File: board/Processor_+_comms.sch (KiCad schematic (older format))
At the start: 43 parts, among them J1 53261-0471, U11 ATXMEGA256A3U-MH, U12 NTS0104, U14 TC1015-3.3VCT713

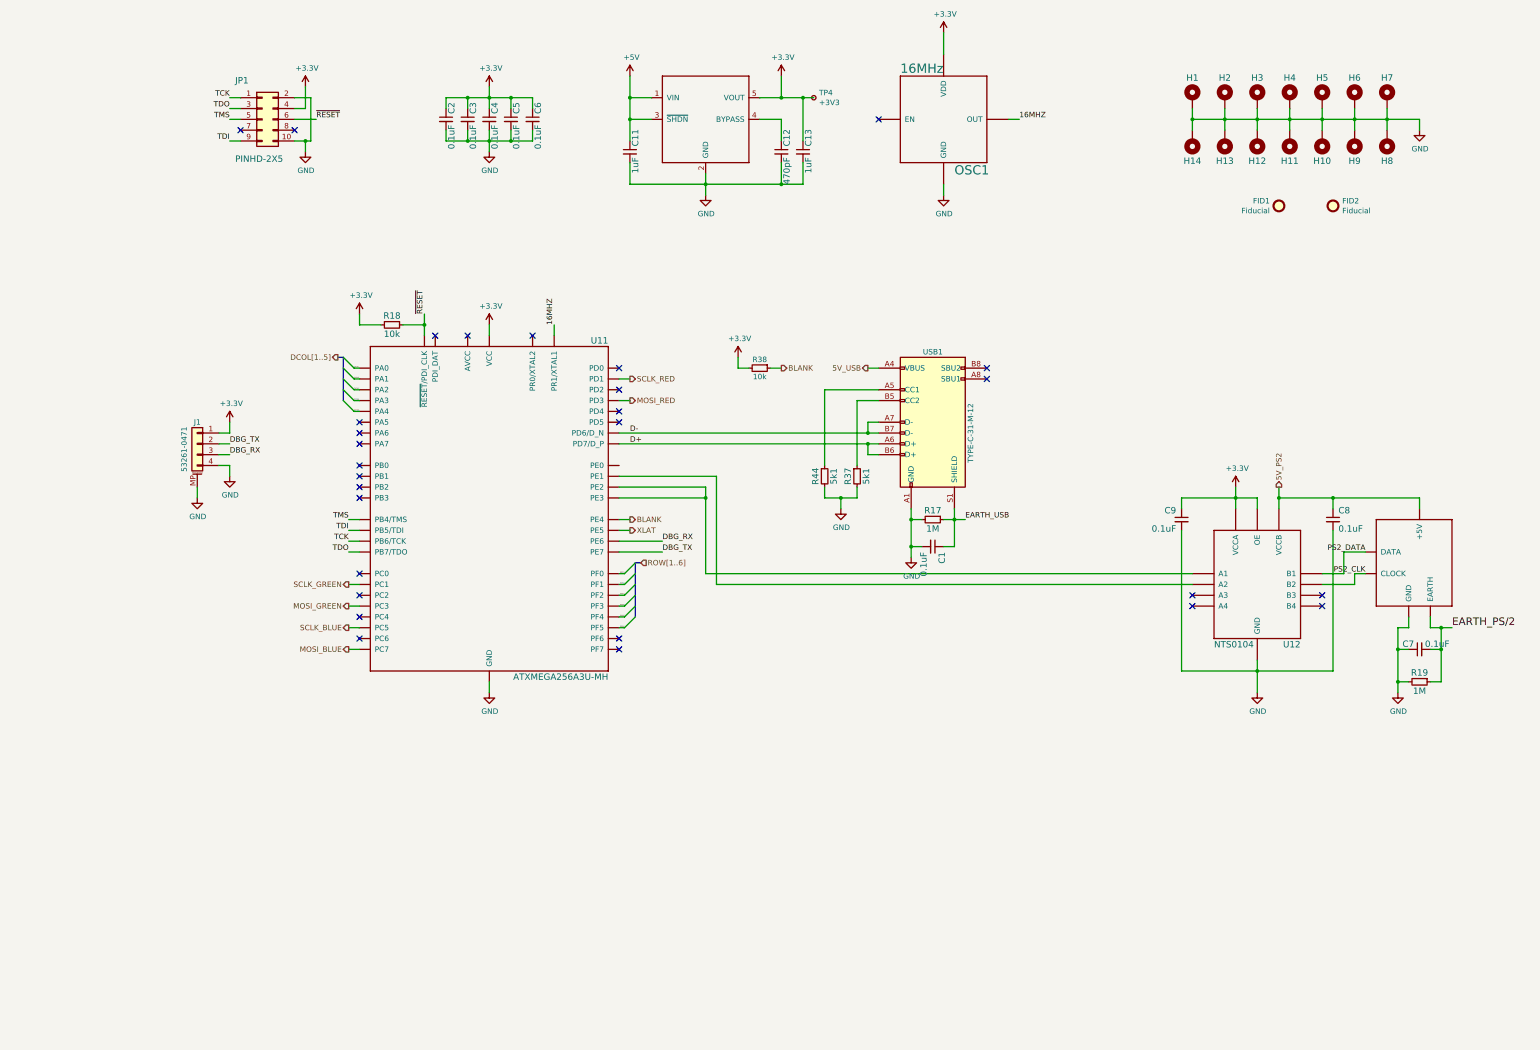
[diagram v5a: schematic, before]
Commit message: Added handling to the board for USB-PD and USB BC v1.2 so we can legally use all 1A we can potentially draw
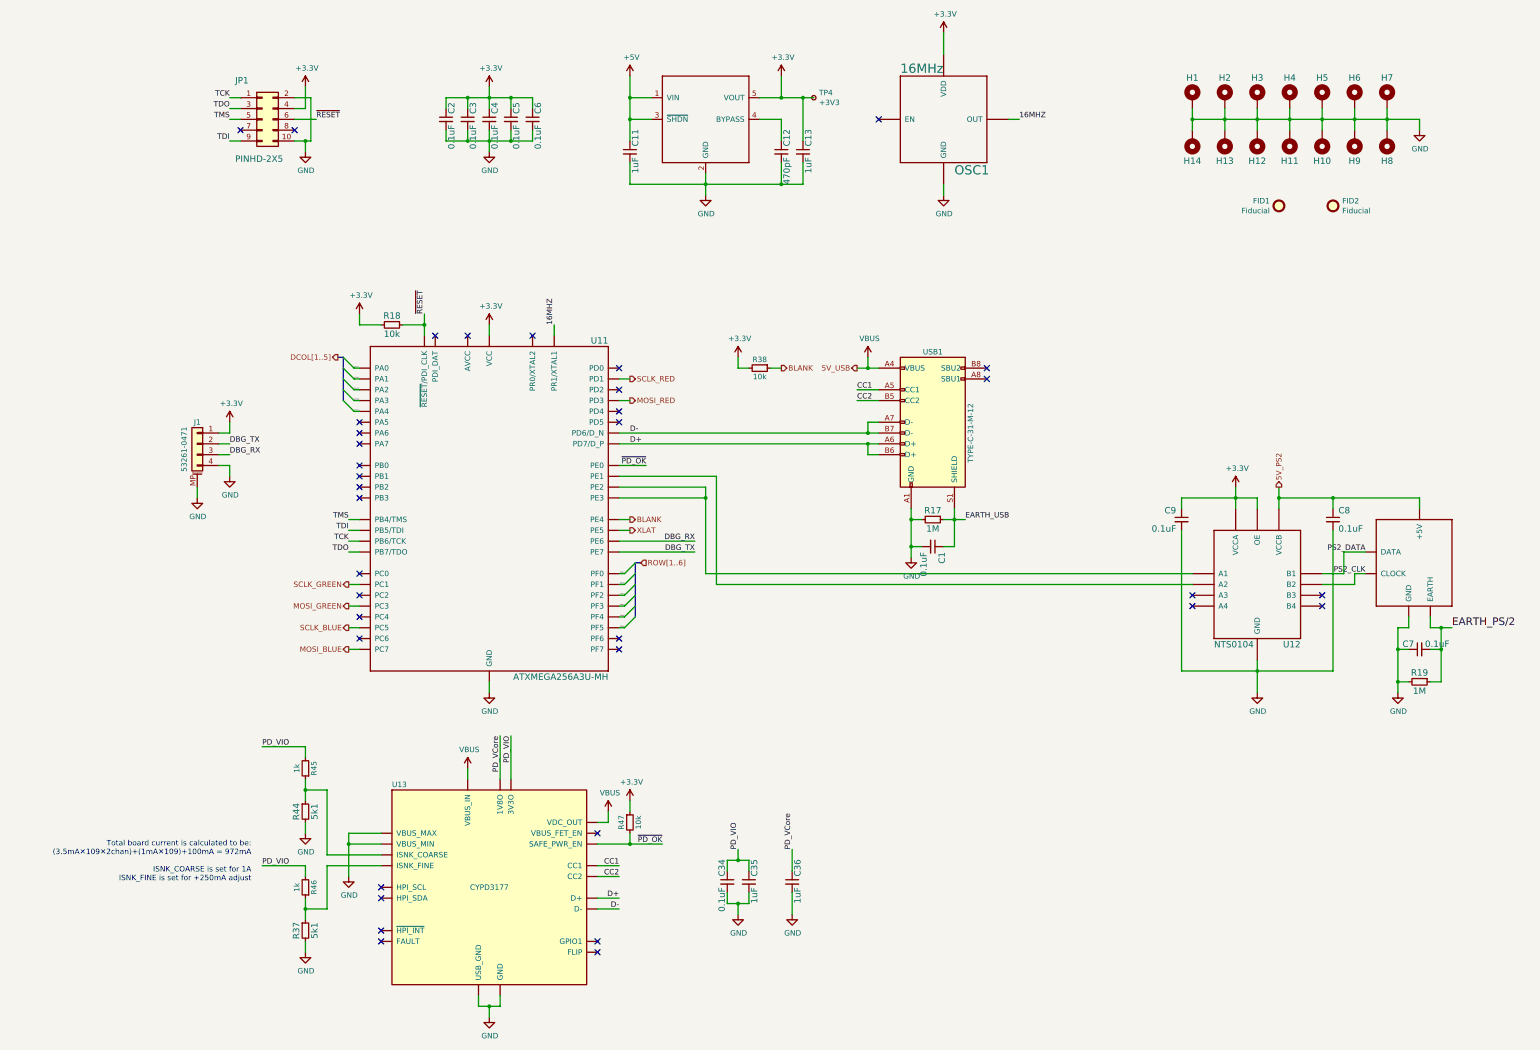
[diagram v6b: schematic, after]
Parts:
- added C34: 0.1uF, rhais_rcl:C0603, symbol Device:C_Small
- added C35, C36: 1uF, rhais_rcl:C0603, symbol Device:C_Small
- added R45, R46: 1k, rhais_rcl:R0603, symbol Device:R_Small
- added R47: 10k, rhais_rcl:R0603, symbol Device:R_Small
- added U13: CYPD3177, rhais_package-qfn:QFN-24-1EP_4x4mm_P0.5mm_EP2.6x2.6mm, symbol DX_MON:CYPD3177
- R37, R44: MPN MCWR06X1003FTL -> MCWR06X5101FTL; OC_FARNELL 2447226 -> 2447404; URL_FARNELL https://uk.farnell.com/multicomp/mcwr06x1003ftl/res-100k-1-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 -> https://uk.farnell.com/multicomp/mcwr06x5101ftl/res-5k1-1-0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
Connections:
- net +3V3: now also R47.1
- net D+: now also U13.17 (D+)
- net D-: now also U13.16 (D-)
- net GND: now also C34.2, C35.2, C36.2, U13.1 (VBUS_MIN), U13.19 (GND), U13.2 (VBUS_MAX), U13.22 (USB_GND), U13.25 (EPAD)
- net ~PD_OK: now reaches U11.36 (PE0)
- net ~PD_OK: now also R47.2, U13.4 (SAFE_PWR_EN)
- net at R44.1: now also R45.1, U13.5 (ISNK_COARSE); no longer USB1.A5 (CC1)
- net at R37.1: now also R46.1, U13.6 (ISNK_FINE); no longer USB1.B5 (CC2)
- net 5V_USB renamed VBUS
- net VBUS: now also U13.11 (VDC_OUT), U13.18 (VBUS_IN)
- new net CC1: U13.15 (CC1), USB1.A5 (CC1)
- new net CC2: U13.14 (CC2), USB1.B5 (CC2)
- new net PD_VCore: C36.1, U13.24 (1V8O)
- new net PD_VIO: C34.1, C35.1, R45.2, R46.2, U13.23 (3V3O)
- no-connect marks 29 -> 36
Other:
- note added: "Total board current is calculated to be:\n(3.5mA✕109✕2chan)+(1mA✕109)+100mA = 972mA\n\nISNK_COARSE is set for 1A\nISNK_FINE is set for +250mA adjust"
- moved on the sheet: R37, R44

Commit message: Fixed some ERC issues
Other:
- moved on the sheet: R38
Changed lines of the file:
@@
 	1    0    0    -1
 $EndComp
-Text HLabel 8400 4500 2    50   Output ~ 0
+Text HLabel 8200 4500 2    50   Output ~ 0
 BLANK
 $Comp
 L Device:R_Small R38
 U 1 1 6F58D17A
-P 8200 4500
-F 0 "R38" V 8150 4500 50  0000 C BNN
-F 1 "10k" V 8250 4500 50  0000 C TNN
-F 2 "rhais_rcl:R0603" H 8200 4500 50  0001 C CNN
-F 3 "http://www.farnell.com/datasheets/2860681.pdf" H 8200 4500 50  0001 C CNN
-F 4 "Multicomp" H 8200 4500 50  0001 C CNN "MFR"
-F 5 "MCWR06X1002FTL" H 8200 4500 50  0001 C CNN "MPN"
-F 6 "2446547" H 8200 4500 50  0001 C CNN "OC_FARNELL"
-F 7 "https://uk.farnell.com/multicomp/mcwr06x1002ftl/res-10k-1-0-1w-0603-thick-film/dp/2446547" H 8200 4500 50  0001 C CNN "URL_FARNELL"
-	1    8200 4500
+P 8000 4500
+F 0 "R38" V 7950 4500 50  0000 C BNN
+F 1 "10k" V 8050 4500 50  0000 C TNN
+F 2 "rhais_rcl:R0603" H 8000 4500 50  0001 C CNN
+F 3 "http://www.farnell.com/datasheets/2860681.pdf" H 8000 4500 50  0001 C CNN
+F 4 "Multicomp" H 8000 4500 50  0001 C CNN "MFR"
+F 5 "MCWR06X1002FTL" H 8000 4500 50  0001 C CNN "MPN"
+F 6 "2446547" H 8000 4500 50  0001 C CNN "OC_FARNELL"
+F 7 "https://uk.farnell.com/multicomp/mcwr06x1002ftl/res-10k-1-0-1w-0603-thick-film/dp/2446547" H 8000 4500 50  0001 C CNN "URL_FARNELL"
+	1    8000 4500
 	0    1    1    0
 $EndComp
 Wire Wire Line
-	8300 4500 8400 4500
+	8100 4500 8200 4500
 $Comp
 L power:+3.3V #PWR043
 U 1 1 6F59EBF8
-P 8000 4400
-F 0 "#PWR043" H 8000 4250 50  0001 C CNN
-F 1 "+3.3V" H 8015 4573 50  0000 C CNN
-F 2 "" H 8000 4400 50  0001 C CNN
-F 3 "" H 8000 4400 50  0001 C CNN
-	1    8000 4400
-	1    0    0    -1
-$EndComp
-Wire Wire Line
-	8100 4500 8000 4500
-Wire Wire Line
-	8000 4500 8000 4400
+P 7800 4400
+F 0 "#PWR043" H 7800 4250 50  0001 C CNN
+F 1 "+3.3V" H 7815 4573 50  0000 C CNN
+F 2 "" H 7800 4400 50  0001 C CNN
+F 3 "" H 7800 4400 50  0001 C CNN
+	1    7800 4400
+	1    0    0    -1
+$EndComp
+Wire Wire Line
+	7900 4500 7800 4500
+Wire Wire Line
+	7800 4500 7800 4400
 Wire Bus Line
 	7050 6300 7100 6300
@@
 Text HLabel 13000 5600 1    50   Output ~ 0
 5V_PS2
-Text HLabel 9100 4500 0    50   Output ~ 0
+Text HLabel 9000 4500 0    50   Output ~ 0
 5V_USB
 NoConn ~ 6900 7100
@@
 Wire Wire Line
 	5800 10400 5800 10300
+Connection ~ 5700 10400
+$Comp
+L power:PWR_FLAG #FLG0102
+U 1 1 5FC40384
+P 9100 4400
+F 0 "#FLG0102" H 9100 4475 50  0001 C CNN
+F 1 "PWR_FLAG" V 9000 4550 50  0000 C CNN
+F 2 "" H 9100 4400 50  0001 C CNN
+F 3 "~" H 9100 4400 50  0001 C CNN
+	1    9100 4400
+	1    0    0    -1
+$EndComp
+Wire Wire Line
+	9100 4400 9100 4500
+Connection ~ 9100 4500
+Wire Wire Line
+	9100 4500 9000 4500
 Wire Bus Line
 	4350 4400 4350 4800
 Wire Bus Line
 	7050 6300 7050 6800
-Connection ~ 5700 10400
 $EndSCHEMATC

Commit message: Done some cleanup in the repo, including adding the case mounting screw specifications to the schematic BOM
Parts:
- H1, H10, H11, H12, H14, H3, H5, H6, H7: MFR (none) -> Accu; MPN (none) -> SHK-M3-20-A2-BL; URL (none) -> https://www.accu.co.uk/en/hexalobular-countersunk-screws/15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
- H13: MFR (none) -> Accu; MPN (none) -> SHP-M3-4-A2-BL; URL (none) -> https://www.accu.co.uk/en/hexalobular-pan-head-screws/15478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
- H2, H4, H8, H9: MFR (none) -> Accu; MPN (none) -> SHP-M3-10-V2-A2-BL; URL (none) -> https://www.accu.co.uk/en/hexalobular-pan-head-screws/47566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
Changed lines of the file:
@@
 F 2 "MountingHole:MountingHole_3.2mm_M3_Pad" H 12200 2000 50  0001 C CNN
 F 3 "" H 12200 2000 50  0001 C CNN
+F 4 "Accu" H 12200 2000 50  0001 C CNN "MFR"
+F 5 "SHK-M3-20-A2-BL" H 12200 2000 50  0001 C CNN "MPN"
+F 6 "https://www.accu.co.uk/en/hexalobular-countersunk-screws/154624-SHK-M3-20-A2-BL" H 12200 2000 50  0001 C CNN "URL"
 	1    12200 2000
 	1    0    0    -1
@@
 F 2 "MountingHole:MountingHole_3.2mm_M3_Pad" H 12500 2000 50  0001 C CNN
 F 3 "" H 12500 2000 50  0001 C CNN
+F 4 "SHP-M3-10-V2-A2-BL" H 12500 2000 50  0001 C CNN "MPN"
+F 5 "Accu" H 12500 2000 50  0001 C CNN "MFR"
+F 6 "https://www.accu.co.uk/en/hexalobular-pan-head-screws/475666-SHP-M3-10-V2-A2-BL" H 12500 2000 50  0001 C CNN "URL"
 	1    12500 2000
 	1    0    0    -1
@@
 F 2 "MountingHole:MountingHole_3.2mm_M3_Pad" H 12800 2000 50  0001 C CNN
 F 3 "" H 12800 2000 50  0001 C CNN
+F 4 "Accu" H 12800 2000 50  0001 C CNN "MFR"
+F 5 "SHK-M3-20-A2-BL" H 12800 2000 50  0001 C CNN "MPN"
+F 6 "https://www.accu.co.uk/en/hexalobular-countersunk-screws/154624-SHK-M3-20-A2-BL" H 12800 2000 50  0001 C CNN "URL"
 	1    12800 2000
 	1    0    0    -1
@@
 F 2 "MountingHole:MountingHole_3.2mm_M3_Pad" H 13100 2000 50  0001 C CNN
 F 3 "" H 13100 2000 50  0001 C CNN
+F 4 "Accu" H 13100 2000 50  0001 C CNN "MFR"
+F 5 "SHP-M3-10-V2-A2-BL" H 13100 2000 50  0001 C CNN "MPN"
+F 6 "https://www.accu.co.uk/en/hexalobular-pan-head-screws/475666-SHP-M3-10-V2-A2-BL" H 13100 2000 50  0001 C CNN "URL"
 	1    13100 2000
 	1    0    0    -1
@@
 F 2 "MountingHole:MountingHole_3.2mm_M3_Pad" H 13400 2000 50  0001 C CNN
 F 3 "" H 13400 2000 50  0001 C CNN
+F 4 "Accu" H 13400 2000 50  0001 C CNN "MFR"
+F 5 "SHK-M3-20-A2-BL" H 13400 2000 50  0001 C CNN "MPN"
+F 6 "https://www.accu.co.uk/en/hexalobular-countersunk-screws/154624-SHK-M3-20-A2-BL" H 13400 2000 50  0001 C CNN "URL"
 	1    13400 2000
 	1    0    0    -1
@@
 F 2 "MountingHole:MountingHole_3.2mm_M3_Pad" H 13700 2000 50  0001 C CNN
 F 3 "" H 13700 2000 50  0001 C CNN
+F 4 "Accu" H 13700 2000 50  0001 C CNN "MFR"
+F 5 "SHK-M3-20-A2-BL" H 13700 2000 50  0001 C CNN "MPN"
+F 6 "https://www.accu.co.uk/en/hexalobular-countersunk-screws/154624-SHK-M3-20-A2-BL" H 13700 2000 50  0001 C CNN "URL"
 	1    13700 2000
 	1    0    0    -1
@@
 F 2 "MountingHole:MountingHole_3.2mm_M3_Pad" H 14000 2000 50  0001 C CNN
 F 3 "" H 14000 2000 50  0001 C CNN
+F 4 "Accu" H 14000 2000 50  0001 C CNN "MFR"
+F 5 "SHK-M3-20-A2-BL" H 14000 2000 50  0001 C CNN "MPN"
+F 6 "https://www.accu.co.uk/en/hexalobular-countersunk-screws/154624-SHK-M3-20-A2-BL" H 14000 2000 50  0001 C CNN "URL"
 	1    14000 2000
 	1    0    0    -1
@@
 F 2 "MountingHole:MountingHole_3.2mm_M3_Pad" H 12200 2400 50  0001 C CNN
 F 3 "" H 12200 2400 50  0001 C CNN
+F 4 "Accu" H 12200 2400 50  0001 C CNN "MFR"
+F 5 "SHK-M3-20-A2-BL" H 12200 2400 50  0001 C CNN "MPN"
+F 6 "https://www.accu.co.uk/en/hexalobular-countersunk-screws/154624-SHK-M3-20-A2-BL" H 12200 2400 50  0001 C CNN "URL"
 	1    12200 2400
 	-1   0    0    1
@@
 F 2 "MountingHole:MountingHole_3.2mm_M3_Pad" H 12500 2400 50  0001 C CNN
 F 3 "" H 12500 2400 50  0001 C CNN
+F 4 "Accu" H 12500 2400 50  0001 C CNN "MFR"
+F 5 "SHP-M3-4-A2-BL" H 12500 2400 50  0001 C CNN "MPN"
+F 6 "https://www.accu.co.uk/en/hexalobular-pan-head-screws/154785-SHP-M3-4-A2-BL" H 12500 2400 50  0001 C CNN "URL"
 	1    12500 2400
 	-1   0    0    1
@@
 F 2 "MountingHole:MountingHole_3.2mm_M3_Pad" H 12800 2400 50  0001 C CNN
 F 3 "" H 12800 2400 50  0001 C CNN
+F 4 "Accu" H 12800 2400 50  0001 C CNN "MFR"
+F 5 "SHK-M3-20-A2-BL" H 12800 2400 50  0001 C CNN "MPN"
+F 6 "https://www.accu.co.uk/en/hexalobular-countersunk-screws/154624-SHK-M3-20-A2-BL" H 12800 2400 50  0001 C CNN "URL"
 	1    12800 2400
 	-1   0    0    1
@@
 F 2 "MountingHole:MountingHole_3.2mm_M3_Pad" H 13100 2400 50  0001 C CNN
 F 3 "" H 13100 2400 50  0001 C CNN
+F 4 "Accu" H 13100 2400 50  0001 C CNN "MFR"
+F 5 "SHK-M3-20-A2-BL" H 13100 2400 50  0001 C CNN "MPN"
+F 6 "https://www.accu.co.uk/en/hexalobular-countersunk-screws/154624-SHK-M3-20-A2-BL" H 13100 2400 50  0001 C CNN "URL"
 	1    13100 2400
 	-1   0    0    1
@@
 F 2 "MountingHole:MountingHole_3.2mm_M3_Pad" H 13400 2400 50  0001 C CNN
 F 3 "" H 13400 2400 50  0001 C CNN
+F 4 "Accu" H 13400 2400 50  0001 C CNN "MFR"
+F 5 "SHK-M3-20-A2-BL" H 13400 2400 50  0001 C CNN "MPN"
+F 6 "https://www.accu.co.uk/en/hexalobular-countersunk-screws/154624-SHK-M3-20-A2-BL" H 13400 2400 50  0001 C CNN "URL"
 	1    13400 2400
 	-1   0    0    1
@@
 F 2 "MountingHole:MountingHole_3.2mm_M3_Pad" H 13700 2400 50  0001 C CNN
 F 3 "" H 13700 2400 50  0001 C CNN
+F 4 "Accu" H 13700 2400 50  0001 C CNN "MFR"
+F 5 "SHP-M3-10-V2-A2-BL" H 13700 2400 50  0001 C CNN "MPN"
+F 6 "https://www.accu.co.uk/en/hexalobular-pan-head-screws/475666-SHP-M3-10-V2-A2-BL" H 13700 2400 50  0001 C CNN "URL"
 	1    13700 2400
 	-1   0    0    1
@@
 F 2 "MountingHole:MountingHole_3.2mm_M3_Pad" H 14000 2400 50  0001 C CNN
 F 3 "" H 14000 2400 50  0001 C CNN
+F 4 "Accu" H 14000 2400 50  0001 C CNN "MFR"
+F 5 "SHP-M3-10-V2-A2-BL" H 14000 2400 50  0001 C CNN "MPN"
+F 6 "https://www.accu.co.uk/en/hexalobular-pan-head-screws/475666-SHP-M3-10-V2-A2-BL" H 14000 2400 50  0001 C CNN "URL"
 	1    14000 2400
 	-1   0    0    1
